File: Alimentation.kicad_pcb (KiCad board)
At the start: 2 copper layers, 50 x 50 mm, 25 parts, among them P1 Prise_Equilibrage, P10 CONN_01X02, P2 Prise_Alim, P3 Prise_Batterie, P4 ConnecteurBippeur, P5 CONN_01X04, P6 CAN_conn, P7 CAN_conn, P8 CONN_01X02, P9 CONN_01X02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

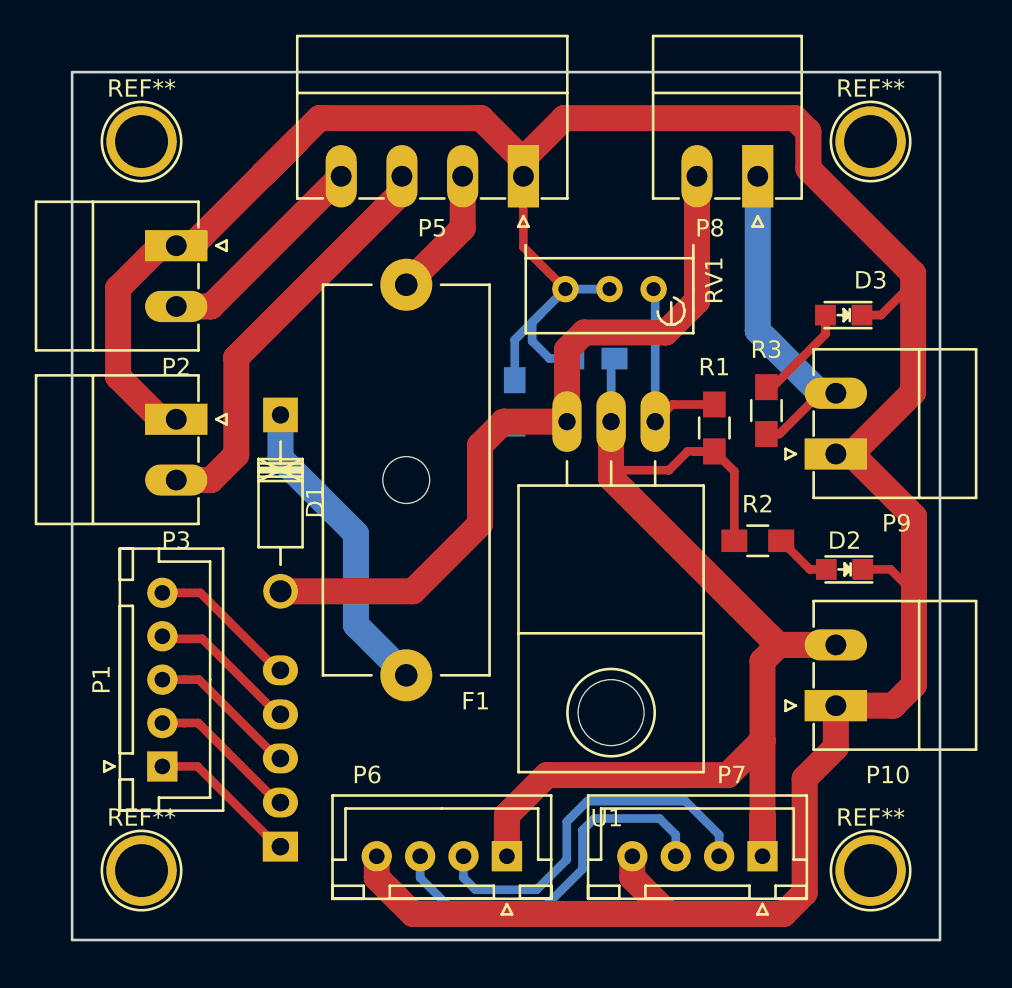
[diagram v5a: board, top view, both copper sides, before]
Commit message: remove useless references for screw holes
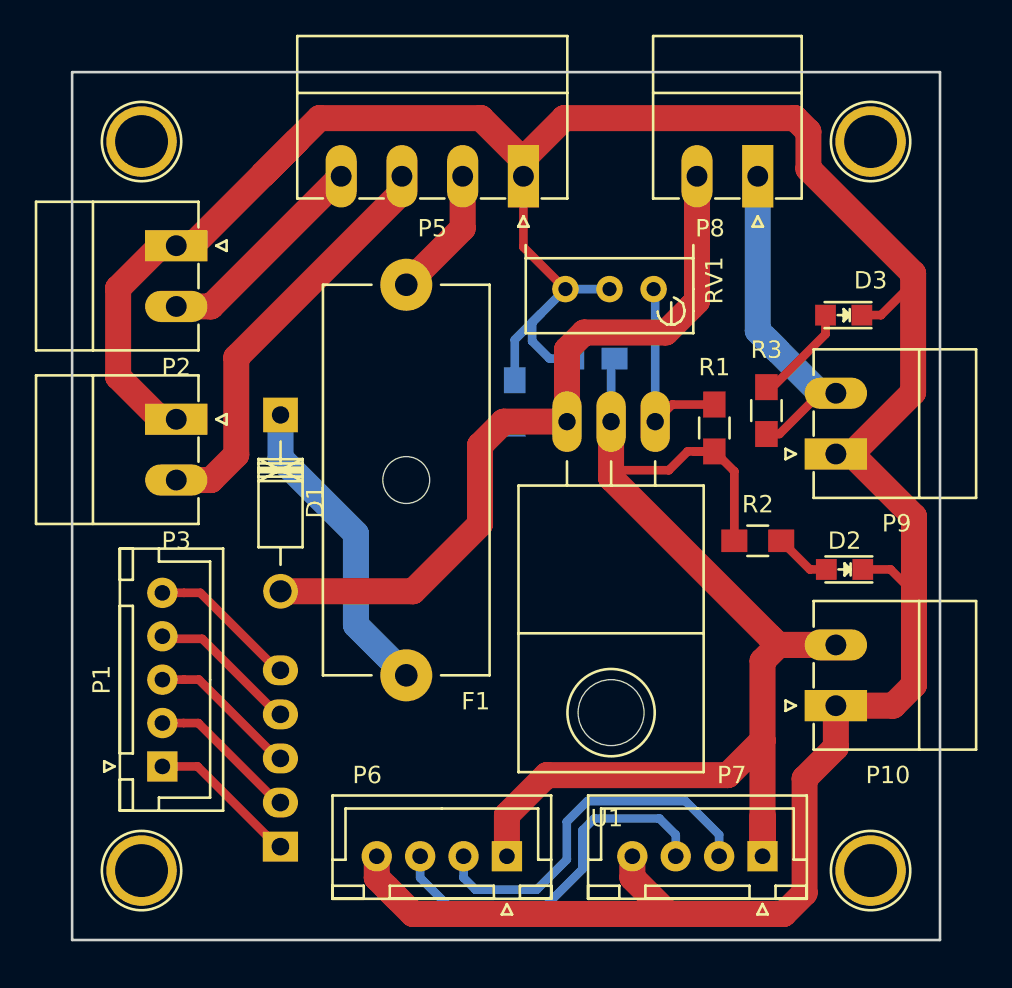
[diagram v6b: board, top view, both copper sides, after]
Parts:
- ? (x4): renamed from REF**; value 1pin -> (none)
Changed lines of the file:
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@@
     (links 38)
     (no_connects 0)
-    (area 99.924999 49.924999 150.075001 100.075001)
+    (area 67.150001 22.3 155.175 100.675)
     (thickness 1.6)
     (drawings 6)
@@
     (descr "module 1 pin (ou trou mecanique de percage)")
     (tags DEV)
-    (fp_text reference REF** (at 0 -3.048) (layer F.SilkS)
-      (effects (font (size 1 1) (thickness 0.15)))
-    )
-    (fp_text value 1pin (at 0 2.794) (layer F.Fab)
+    (fp_text reference "" (at 0 -3.048) (layer F.SilkS)
+      (effects (font (size 1 1) (thickness 0.15)))
+    )
+    (fp_text value "" (at 0 2.794) (layer F.Fab)
       (effects (font (size 1 1) (thickness 0.15)))
     )
@@
     (descr "module 1 pin (ou trou mecanique de percage)")
     (tags DEV)
-    (fp_text reference REF** (at 0 -3.048) (layer F.SilkS)
-      (effects (font (size 1 1) (thickness 0.15)))
-    )
-    (fp_text value 1pin (at 0 2.794) (layer F.Fab)
+    (fp_text reference "" (at 0 -3.048) (layer F.SilkS)
+      (effects (font (size 1 1) (thickness 0.15)))
+    )
+    (fp_text value "" (at 0 2.794) (layer F.Fab)
       (effects (font (size 1 1) (thickness 0.15)))
     )
@@
     (descr "module 1 pin (ou trou mecanique de percage)")
     (tags DEV)
-    (fp_text reference REF** (at 0 -3.048) (layer F.SilkS)
-      (effects (font (size 1 1) (thickness 0.15)))
-    )
-    (fp_text value 1pin (at 0 2.794) (layer F.Fab)
+    (fp_text reference "" (at 0 -3.048) (layer F.SilkS)
+      (effects (font (size 1 1) (thickness 0.15)))
+    )
+    (fp_text value "" (at 0 2.794) (layer F.Fab)
       (effects (font (size 1 1) (thickness 0.15)))
     )
@@
     (descr "module 1 pin (ou trou mecanique de percage)")
     (tags DEV)
-    (fp_text reference REF** (at 0 -3.048) (layer F.SilkS)
-      (effects (font (size 1 1) (thickness 0.15)))
-    )
-    (fp_text value 1pin (at 0 2.794) (layer F.Fab)
-      (effects (font (size 1 1) (thickness 0.15)))
-    )
+    (fp_text reference "" (at 0 -3.048) (layer F.SilkS)
+      (effects (font (size 1 1) (thickness 0.15)))
+    )
+    (fp_text value "" (at 0 2.794) (layer F.Fab)
+      (effects (font (size 1 1) (thickness 0.15)))
+    )

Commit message: déplace les deux connecteurs de sortie
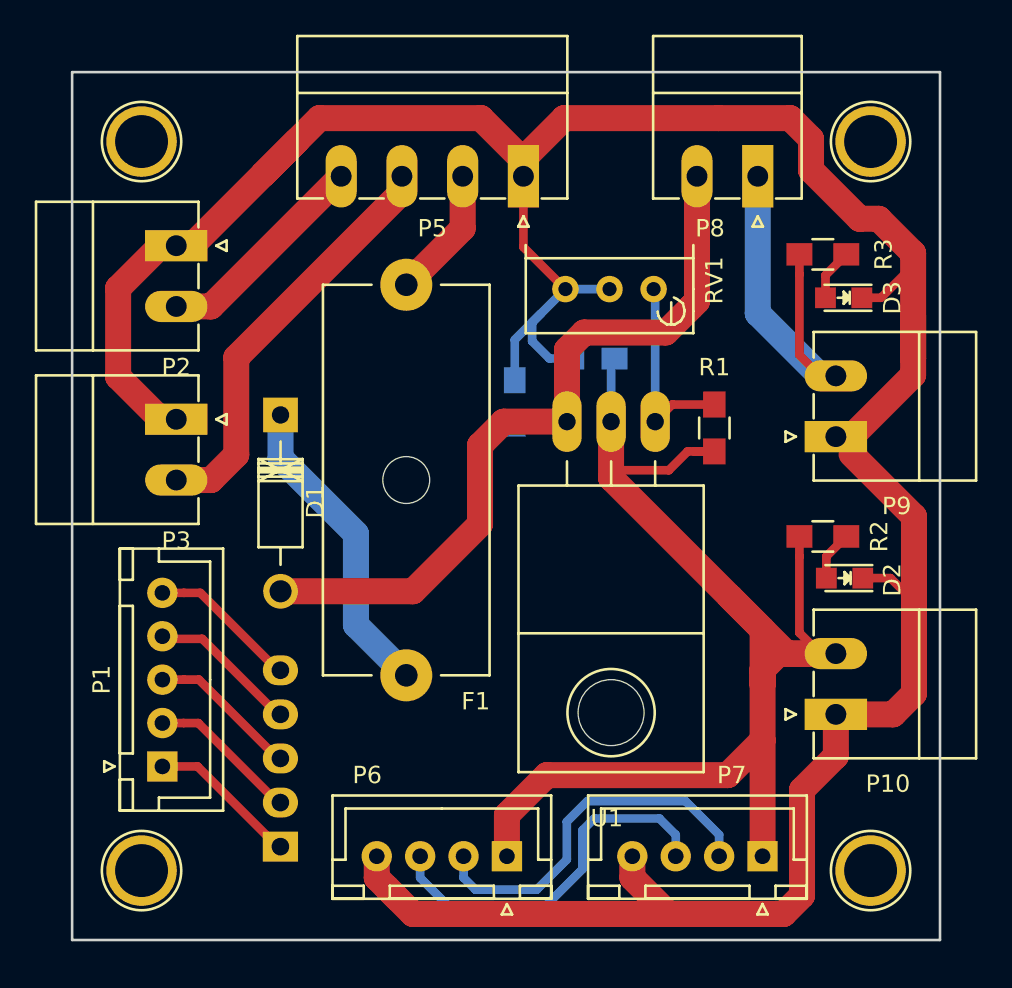
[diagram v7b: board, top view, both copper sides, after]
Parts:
- moved R3 9.57 mm to (143.2, 60.5), turned to 0 degrees
- moved R2 3.76 mm to (143.2, 76.8)
- moved D3 1.00 mm to (144.5, 63.0)
- moved P9 1.00 mm to (144.0, 71.0)
- moved D2 0.50 mm to (144.5, 79.2)
- moved P10 0.50 mm to (144.0, 87.0)
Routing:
- net +9V: track 78.9 -> 83.3 mm
- net Net-(D3-Pad2): track 5.76 -> 3.00 mm
- net GND: track 176.8 -> 178.7 mm
- net Non_régulé: track 20.7 -> 22.3 mm

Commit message: recentre le régul
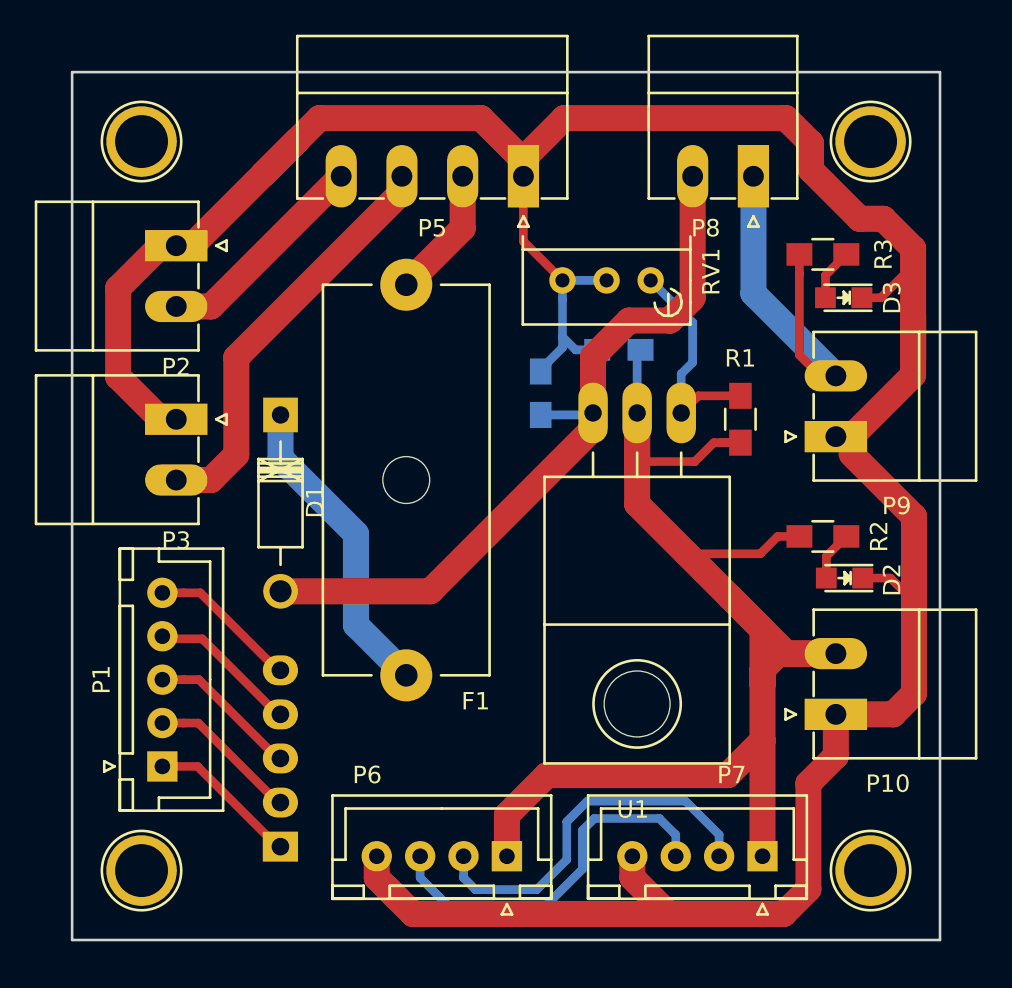
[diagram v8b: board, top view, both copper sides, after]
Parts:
- moved C1 1.58 mm to (127.0, 68.5)
- moved C2 1.58 mm to (131.5, 66.0)
- moved R1 1.58 mm to (138.5, 70.0)
- moved U1 1.58 mm to (132.6, 69.6)
- moved RV1 0.53 mm to (133.3, 62.0)
- moved P8 0.25 mm to (139.2, 56.0)
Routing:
- net +9V: track 83.3 -> 86.1 mm
- net GND: track 178.7 -> 176.2 mm
- net Net-(C1-Pad1): track 46.8 -> 45.5 mm
- net Net-(R1-Pad2): track 12.6 -> 13.8 mm
